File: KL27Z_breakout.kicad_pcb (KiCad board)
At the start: 2 copper layers, 12 x 55 mm, 15 parts, among them J1 USB_mini_micro_B, P1 CONN_01X08, P2 CONN_01X08, P3 CONN_01X08, P4 CONN_01X08, SW1 SW_PUSH, SW2 SW_PUSH, U1 MKL27Z256VFM4

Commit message: Save some works
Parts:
- P1, P2, P3, P4: footprint Pin_Headers:Pin_Header_Straight_1x08 -> keyboard_parts:Pin_Header_Straight_1x08
- moved C3 43.6 mm to (105.8, 138.5)
- moved C2 42.5 mm to (101.0, 129.5), turned to 90 degrees
- moved C4 41.8 mm to (101.0, 134.5), turned to 270 degrees
- moved SW1 39.7 mm to (106.0, 155.0), turned to 270 degrees
- moved SW2 35.6 mm to (106.0, 148.4), turned to 90 degrees
- moved C1 23.9 mm to (102.1, 106.0), turned to 0 degrees
- moved R1 16.3 mm to (105.0, 124.0)
- moved R2 16.3 mm to (107.0, 124.0)
- moved P2 12.2 mm to (102.2, 147.1)
- moved P1 9.19 mm to (102.2, 116.9)
- moved P4 8.81 mm to (109.8, 116.9)
- moved P3 6.06 mm to (109.8, 147.1)
- moved U1 2.42 mm to (106.0, 132.0)
- moved SJ1 0.16 mm to (104.0, 109.3)
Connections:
- P1 pad 8: PTE0 -> (no net)
- P2 pad 8: GND -> PTA18
- P3 pad 1: PTA18 -> PTA19
- P3 pad 2: PTA19 -> PTA20
- P3 pad 3: PTA20 -> PTB0
- P3 pad 4: PTB0 -> PTB1
- P3 pad 5: PTB1 -> PTC1
- P3 pad 6: PTC1 -> PTC2
- P3 pad 7: PTC2 -> PTC3
- P3 pad 8: PTC3 -> PTC4
- P4 pad 1: PTC4 -> PTC5
- P4 pad 2: PTC5 -> PTC6
- P4 pad 3: PTC6 -> PTC7
- P4 pad 4: PTC7 -> PTD4
- P4 pad 5: PTD4 -> PTD5
- P4 pad 6: PTD5 -> PTD6
- P4 pad 7: PTD6 -> PTD7
- P4 pad 8: PTD7 -> PTE0
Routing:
- net PTE0: track 4.33 -> 25.1 mm
- net Net-(J1-Pad2): track 0.00 -> 19.5 mm
- net Net-(J1-Pad3): track 0.00 -> 19.4 mm
- net +3V3: track 0.07 -> 16.4 mm, vias 0 -> 1
- net PTD4: track 0.00 -> 15.1 mm, vias 0 -> 1
- net Net-(R1-Pad1): track 20.0 -> 5.40 mm, vias 0 -> 2
- net PTC7: track 0.00 -> 13.3 mm, vias 0 -> 1
- net Net-(R2-Pad1): track 20.3 -> 7.76 mm
- net PTC6: track 0.00 -> 11.1 mm, vias 0 -> 1
- net PTC4: track 0.00 -> 7.92 mm
- net PTC5: track 0.00 -> 7.53 mm, vias 0 -> 1
- net VBUS: track 0.00 -> 6.96 mm
- net PTA19: track 20.9 -> 25.6 mm
- net VREGIN: track 21.2 -> 25.6 mm, vias 0 -> 1
- net PTC3: track 7.27 -> 11.5 mm, vias 0 -> 1
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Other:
- board size 12 x 55 mm -> 12 x 60 mm

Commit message: 400mil pcb
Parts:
- P1, P4: value CONN_01X08 -> CONN_01X06; footprint keyboard_parts:Pin_Header_Straight_1x08 -> keyboard_parts:Pin_Header_Straight_1x06
- moved C2 21.9 mm to (103.2, 107.7)
- moved R1 20.4 mm to (107.3, 103.7)
- moved R2 20.3 mm to (105.3, 103.7)
- moved SW2 19.5 mm to (105.1, 129.0)
- moved SW1 19.0 mm to (105.1, 136.1)
- moved P2 18.0 mm to (100.0, 129.2)
- moved C4 18.0 mm to (99.9, 116.5)
- moved P3 17.9 mm to (110.2, 129.2)
- moved U1 15.5 mm to (105.1, 116.5)
- moved C3 15.3 mm to (104.6, 123.2), turned to 270 degrees
- moved P1 10.8 mm to (100.0, 106.3)
- moved P4 10.5 mm to (110.2, 106.3)
- moved SJ1 8.40 mm to (101.5, 101.3)
- moved J1 6.63 mm to (105.1, 94.9)
- moved C1 2.52 mm to (103.2, 103.7), turned to 270 degrees
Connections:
- J1 pad 4: (no net) -> Net-(J1-Pad4)
- P1 pad 3: +3V3 -> PTD5
- P1 pad 4: PTA0 -> PTD6
- P1 pad 5: PTA3 -> PTD7
- P1 pad 6: PTA20 -> PTE0
- P3 pad 8: PTC4 -> GND
- P4 pad 1: PTC5 -> PTC4
- P4 pad 2: PTC6 -> PTC5
- P4 pad 3: PTC7 -> PTC6
- P4 pad 4: PTD4 -> PTC7
- P4 pad 5: PTD5 -> PTD4
- P4 pad 6: PTD6 -> GND
- U1 pad 33: (no net) -> GND
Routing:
- net GND: track 1.19 -> 80.7 mm, vias 1 -> 22
- net PTE0: track 25.1 -> 4.98 mm
- net Net-(J1-Pad3): track 19.4 -> 5.38 mm, vias 0 -> 2
- net PTD7: track 21.7 -> 8.04 mm
- net Net-(J1-Pad2): track 19.5 -> 7.25 mm
- net +3V3: track 16.4 -> 26.3 mm, vias 1 -> 3
- net PTD6: track 19.9 -> 11.7 mm
- net VREGIN: track 25.6 -> 18.9 mm, vias 1 -> 0
- net Net-(R1-Pad1): track 5.40 -> 11.9 mm, vias 2 -> 0
- net PTC3: track 11.5 -> 7.45 mm, vias 1 -> 0
- net PTC2: track 13.4 -> 9.71 mm, vias 1 -> 0
- net PTA0: track 13.4 -> 10.0 mm
- net Net-(R2-Pad1): track 7.76 -> 11.1 mm
- net PTA2: track 18.0 -> 14.7 mm
- net PTA3: track 20.3 -> 17.0 mm
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- added copper zone on B.Cu, net GND
- added copper zone on F.Cu, net GND
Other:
- board size 12 x 60 mm -> 13.7 x 46.4 mm

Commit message: Save 300mil work
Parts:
- moved C3 12.1 mm to (92.6, 121.1)
- moved C1 10.3 mm to (93.1, 105.6)
- moved C2 8.93 mm to (94.9, 110.9)
- moved C4 7.24 mm to (92.6, 116.5)
- moved P3 3.59 mm to (107.6, 131.8)
- moved SW2 3.54 mm to (103.8, 132.3)
- moved SW1 3.07 mm to (103.8, 138.9)
- moved P4 2.84 mm to (107.6, 107.6)
- moved U1 2.84 mm to (103.8, 119.0)
- moved R1 2.70 mm to (104.8, 104.8)
- moved R2 2.70 mm to (102.8, 104.8)
- moved P2 2.54 mm to (100.0, 131.8)
- moved P1 1.27 mm to (100.0, 107.6)
- moved J1 1.27 mm to (103.8, 94.9)
- moved SJ1 0.76 mm to (102.3, 101.3)
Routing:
- net (no net): track 0.00 -> 464.9 mm, vias 0 -> 31
- net GND: track 80.7 -> 0.00 mm, vias 22 -> 0
- net +3V3: track 26.3 -> 0.00 mm, vias 3 -> 0
- net PTA19: track 22.8 -> 0.00 mm
- net PTA18: track 22.6 -> 0.00 mm
- net PTA20: track 20.8 -> 0.00 mm
- net PTA4: track 19.7 -> 0.00 mm
- net VREGIN: track 18.9 -> 0.00 mm
- net PTB0: track 17.4 -> 0.00 mm
- net PTA3: track 17.0 -> 0.00 mm
- net PTD5: track 15.1 -> 0.00 mm, vias 1 -> 0
- net PTB1: track 15.0 -> 0.00 mm
- net PTA2: track 14.7 -> 0.00 mm
- net PTD4: track 14.2 -> 0.00 mm
- net PTA1: track 12.3 -> 0.00 mm
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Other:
- board size 13.7 x 46.4 mm -> 13.8 x 46.4 mm

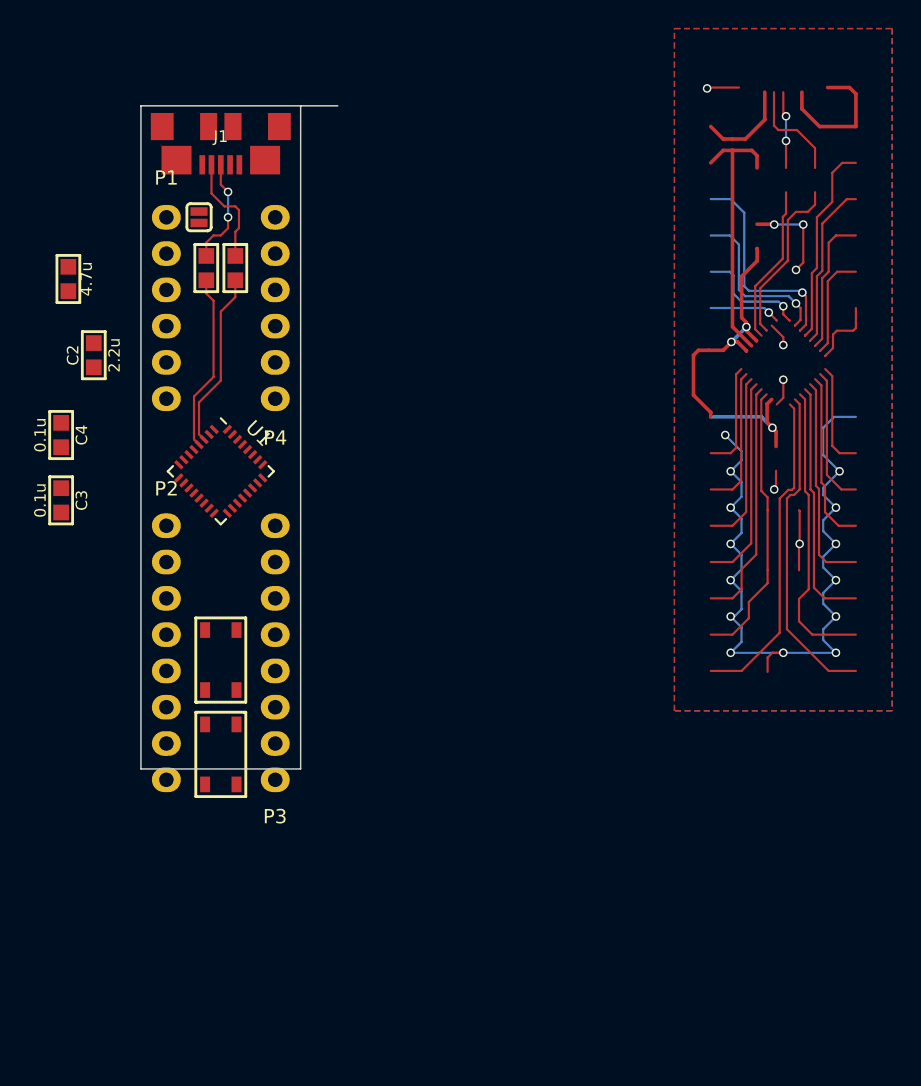
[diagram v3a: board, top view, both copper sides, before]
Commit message: Route traces for 300mil PCB
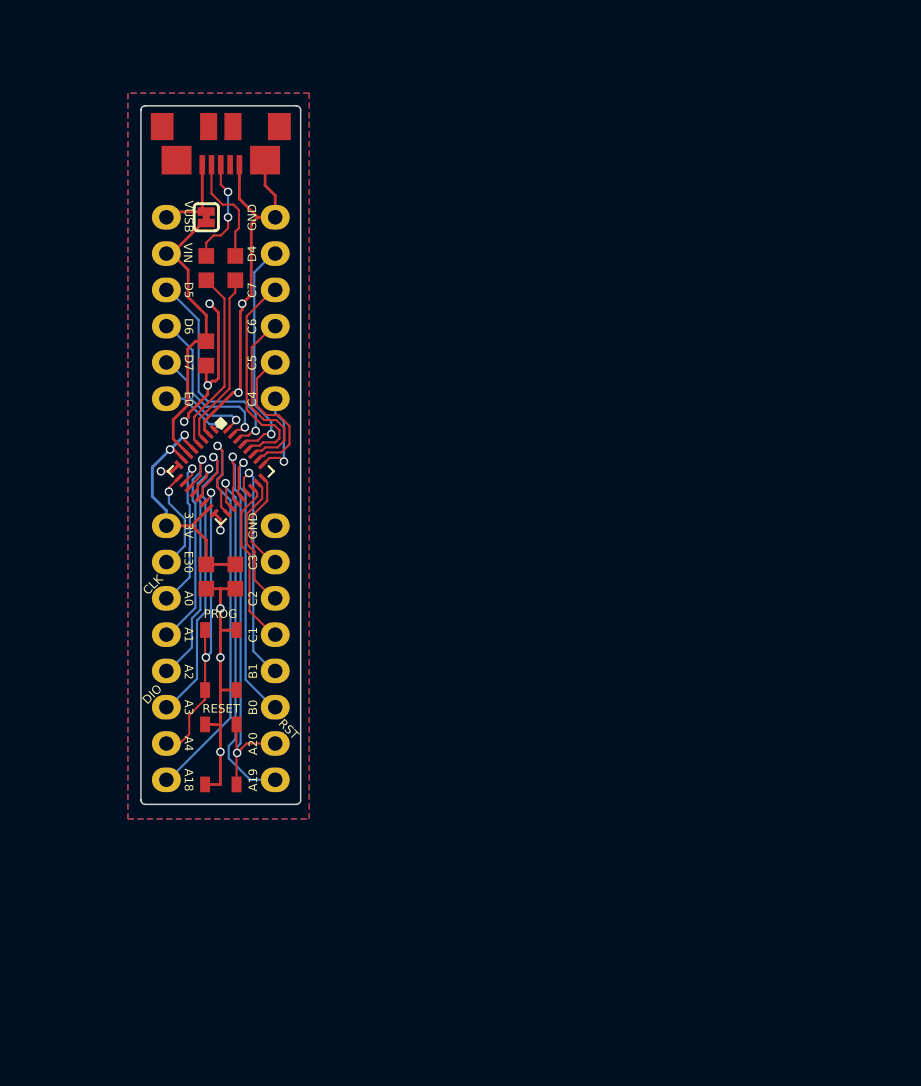
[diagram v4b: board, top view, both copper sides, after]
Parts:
- removed C3: 0.1u, keyboard_parts:C_1608
- SJ1: footprint keyboard_parts:SOLDER_JUMPER_2 -> keyboard_parts:SOLDER_JUMPER_2_WIRED
- moved C2 17.4 mm to (102.8, 126.4), turned to 270 degrees
- moved C4 15.7 mm to (104.8, 126.4)
- moved C1 11.0 mm to (102.8, 110.8)
- moved SJ1 0.51 mm to (102.8, 101.3)
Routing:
- net (no net): track 464.9 -> 0.00 mm, vias 31 -> 0
- net GND: track 0.00 -> 62.1 mm, vias 0 -> 10
- net PTA20: track 0.00 -> 31.7 mm, vias 0 -> 2
- net PTA18: track 0.00 -> 31.3 mm, vias 0 -> 1
- net PTA19: track 0.00 -> 25.6 mm, vias 0 -> 1
- net PTA3: track 0.00 -> 22.9 mm, vias 0 -> 1
- net PTA4: track 0.00 -> 22.3 mm, vias 0 -> 2
- net PTB0: track 0.00 -> 21.1 mm, vias 0 -> 1
- net VREGIN: track 0.00 -> 20.6 mm
- net +3V3: track 0.00 -> 19.0 mm, vias 0 -> 2
- net PTA2: track 0.00 -> 17.8 mm, vias 0 -> 1
- net PTB1: track 0.00 -> 16.4 mm, vias 0 -> 1
- net PTD4: track 0.00 -> 16.1 mm, vias 0 -> 1
- net PTA1: track 0.00 -> 15.9 mm, vias 0 -> 1
- net PTD5: track 0.00 -> 15.6 mm, vias 0 -> 1
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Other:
- board size 13.8 x 46.4 mm -> 11.2 x 48.9 mm
- rule pad_to_mask_clearance: 0.2 -> 0.05
- board text added: "3.3V"
- board text added: "A0"
- board text added: "A1"
- board text added: "A18"
- board text added: "A19"
- board text added: "A2"
- board text added: "A20"
- board text added: "A3"
- board text added: "A4"
- board text added: "B0"
- board text added: "B1"
- board text added: "C1"
- board text added: "C2"
- board text added: "C3"
- board text added: "C4"
- board text added: "C5"
- board text added: "C6"
- board text added: "C7"
- board text added: "CLK"
- board text added: "D4"
- board text added: "D5"
- board text added: "D6"
- board text added: "D7"
- board text added: "DIO"
- board text added: "E0"
- board text added: "E30"
- board text added: "GND"
- board text added: "KL27Z breakout TMK 2016/07"
- board text added: "PROG"
- board text added: "RESET"
- board text added: "RST"
- board text added: "VIN"
- board text added: "VUSB"

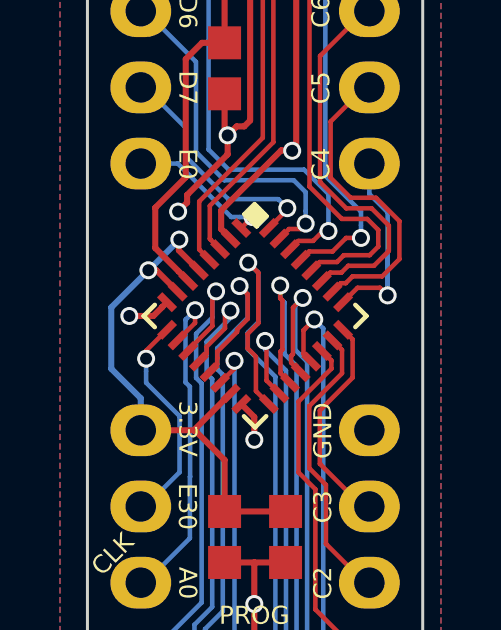
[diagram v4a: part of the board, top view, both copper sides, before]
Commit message: Add silk screen fill under thermal pad
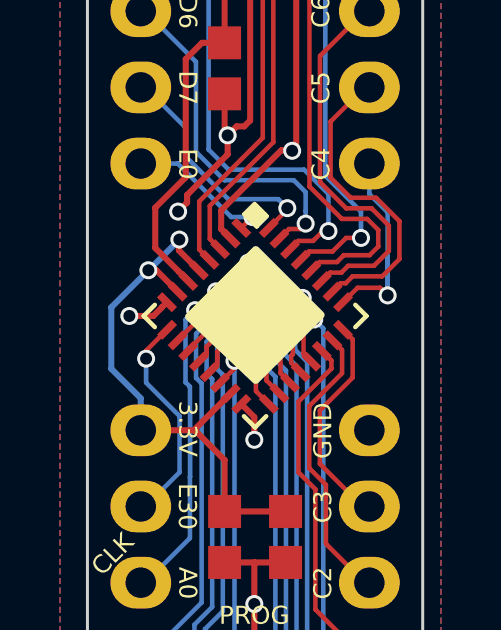
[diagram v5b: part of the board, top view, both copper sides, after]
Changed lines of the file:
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@@
   (general
     (links 57)
-    (no_connects 1)
-    (area 94.881667 86.8546 120.440115 145.865)
+    (no_connects 0)
+    (area 98.171999 93.419999 109.448001 142.410001)
     (thickness 1.6)
     (drawings 72)
@@
     (34 B.Paste user)
     (35 F.Paste user)
-    (36 B.SilkS user hide)
+    (36 B.SilkS user)
     (37 F.SilkS user)
     (38 B.Mask user)
@@
     (visible_elements FFFFEF7F)
     (pcbplotparams
-      (layerselection 0x010f8_80000001)
+      (layerselection 0x010f0_80000001)
       (usegerberextensions true)
       (excludeedgelayer true)
@@
     (add_net VBUS)
     (add_net VREGIN)
-  )
-  (module keyboard_parts:USB_microB (layer F.Cu)
-    (at 103.81 94.92 180)
-    (descr "USB microB hirose ZX62R-B-5P")
-    (tags "USB micorB hirose")
-    (fp_text reference J1 (at 0 -0.6985 180) (layer F.SilkS) hide
-      (effects (font (size 0.8128 0.8128) (thickness 0.2032)))
-    )
-    (fp_text value USB_mini_micro_B (at 0 0.22606 180) (layer F.SilkS) hide
-      (effects (font (size 0.6 0.6) (thickness 0.15)))
-    )
-    (fp_text user "PCB edge" (at -0.05 1.45 180) (layer Dwgs.User) hide
-      (effects (font (size 0.5 0.5) (thickness 0.125)))
-    )
-    (fp_line (start 3.75 2.15) (end 4.25 2.75) (layer Dwgs.User) (width 0.2))
-    (fp_line (start -3.75 2.15) (end -4.25 2.675) (layer Dwgs.User) (width 0.2))
-    (fp_line (start -3 1.45) (end 3 1.45) (layer Dwgs.User) (width 0.2))
-    (fp_line (start -3.75 2.15) (end -3.75 1.35) (layer Dwgs.User) (width 0.2))
-    (fp_line (start -3.75 2.15) (end 3.75 2.15) (layer Dwgs.User) (width 0.2))
-    (fp_line (start 3.75 2.15) (end 3.75 1.35) (layer Dwgs.User) (width 0.2))
-    (pad 6 smd rect (at 0.85 0 180) (size 1.2 1.9) (layers F.Cu F.Paste F.Mask))
-    (pad 1 smd rect (at 1.29794 -2.67462) (size 0.4 1.35) (layers F.Cu F.Paste F.Mask)
-      (net 4 VBUS) (clearance 0.1))
-    (pad 6 smd rect (at -3.0988 -2.3495 180) (size 2.1 2) (layers F.Cu F.Paste F.Mask)
-      (net 1 GND))
-    (pad 6 smd rect (at 3.0988 -2.3495 180) (size 2.1 2) (layers F.Cu F.Paste F.Mask)
-      (net 1 GND))
-    (pad 6 smd rect (at -4.09956 0 180) (size 1.6 1.9) (layers F.Cu F.Paste F.Mask)
-      (net 1 GND))
-    (pad 6 smd rect (at 4.09956 0 180) (size 1.6 1.9) (layers F.Cu F.Paste F.Mask)
-      (net 1 GND))
-    (pad 2 smd rect (at 0.65024 -2.67462) (size 0.4 1.35) (layers F.Cu F.Paste F.Mask)
-      (net 5 "Net-(J1-Pad2)") (clearance 0.1))
-    (pad 3 smd rect (at 0 -2.67462) (size 0.4 1.35) (layers F.Cu F.Paste F.Mask)
-      (net 6 "Net-(J1-Pad3)") (clearance 0.1))
-    (pad 4 smd rect (at -0.65024 -2.67462) (size 0.4 1.35) (layers F.Cu F.Paste F.Mask)
-      (net 32 "Net-(J1-Pad4)") (clearance 0.1))
-    (pad 5 smd rect (at -1.30048 -2.67462) (size 0.4 1.35) (layers F.Cu F.Paste F.Mask)
-      (net 1 GND) (clearance 0.1))
-    (pad 6 smd rect (at -0.85 0 180) (size 1.2 1.9) (layers F.Cu F.Paste F.Mask))
   )
   (module Housings_DFN_QFN:QFN-32-1EP_5x5mm_Pitch0.5mm locked (layer F.Cu)
@@
     (pad 32 smd rect (at -1.75 -2.4 45) (size 0.7 0.25) (layers F.Cu F.Paste F.Mask)
       (net 29 PTD7))
-    (pad "" smd rect (at 0 0 315) (size 3.5 3.5) (layers F.SilkS))
     (model Housings_DFN_QFN.3dshapes/QFN-32-1EP_5x5mm_Pitch0.5mm.wrl
       (at (xyz 0 0 0))
@@
       (rotate (xyz 0 0 0))
     )
+  )
+  (module keyboard_parts:USB_microB (layer F.Cu)
+    (at 103.81 94.92 180)
+    (descr "USB microB hirose ZX62R-B-5P")
+    (tags "USB micorB hirose")
+    (fp_text reference J1 (at 0 -0.6985 180) (layer F.SilkS) hide
+      (effects (font (size 0.8128 0.8128) (thickness 0.2032)))
+    )
+    (fp_text value USB_mini_micro_B (at 0 0.22606 180) (layer F.SilkS) hide
+      (effects (font (size 0.6 0.6) (thickness 0.15)))
+    )
+    (fp_text user "PCB edge" (at -0.05 1.45 180) (layer Dwgs.User) hide
+      (effects (font (size 0.5 0.5) (thickness 0.125)))
+    )
+    (fp_line (start 3.75 2.15) (end 4.25 2.75) (layer Dwgs.User) (width 0.2))
+    (fp_line (start -3.75 2.15) (end -4.25 2.675) (layer Dwgs.User) (width 0.2))
+    (fp_line (start -3 1.45) (end 3 1.45) (layer Dwgs.User) (width 0.2))
+    (fp_line (start -3.75 2.15) (end -3.75 1.35) (layer Dwgs.User) (width 0.2))
+    (fp_line (start -3.75 2.15) (end 3.75 2.15) (layer Dwgs.User) (width 0.2))
+    (fp_line (start 3.75 2.15) (end 3.75 1.35) (layer Dwgs.User) (width 0.2))
+    (pad 6 smd rect (at 0.85 0 180) (size 1.2 1.9) (layers F.Cu F.Paste F.Mask))
+    (pad 1 smd rect (at 1.29794 -2.67462) (size 0.4 1.35) (layers F.Cu F.Paste F.Mask)
+      (net 4 VBUS) (clearance 0.1))
+    (pad 6 smd rect (at -3.0988 -2.3495 180) (size 2.1 2) (layers F.Cu F.Paste F.Mask)
+      (net 1 GND))
+    (pad 6 smd rect (at 3.0988 -2.3495 180) (size 2.1 2) (layers F.Cu F.Paste F.Mask)
+      (net 1 GND))
+    (pad 6 smd rect (at -4.09956 0 180) (size 1.6 1.9) (layers F.Cu F.Paste F.Mask)
+      (net 1 GND))
+    (pad 6 smd rect (at 4.09956 0 180) (size 1.6 1.9) (layers F.Cu F.Paste F.Mask)
+      (net 1 GND))
+    (pad 2 smd rect (at 0.65024 -2.67462) (size 0.4 1.35) (layers F.Cu F.Paste F.Mask)
+      (net 5 "Net-(J1-Pad2)") (clearance 0.1))
+    (pad 3 smd rect (at 0 -2.67462) (size 0.4 1.35) (layers F.Cu F.Paste F.Mask)
+      (net 6 "Net-(J1-Pad3)") (clearance 0.1))
+    (pad 4 smd rect (at -0.65024 -2.67462) (size 0.4 1.35) (layers F.Cu F.Paste F.Mask)
+      (net 32 "Net-(J1-Pad4)") (clearance 0.1))
+    (pad 5 smd rect (at -1.30048 -2.67462) (size 0.4 1.35) (layers F.Cu F.Paste F.Mask)
+      (net 1 GND) (clearance 0.1))
+    (pad 6 smd rect (at -0.85 0 180) (size 1.2 1.9) (layers F.Cu F.Paste F.Mask))
   )
   (module keyboard_parts:C_1608 placed (layer F.Cu)
@@
       )
     )
+  )
+  (zone (net 0) (net_name "") (layer F.SilkS) (hatch edge 0.508)
+    (connect_pads (clearance 0.2))
+    (min_thickness 0.254)
+    (fill yes (arc_segments 16) (thermal_gap 0.508) (thermal_bridge_width 0.508))
+    (polygon
+      (pts
+        (xy 103.8326 116.6667) (xy 106.1821 119.0162) (xy 103.8326 121.3657) (xy 101.4196 119.0797)
+      )
+    )

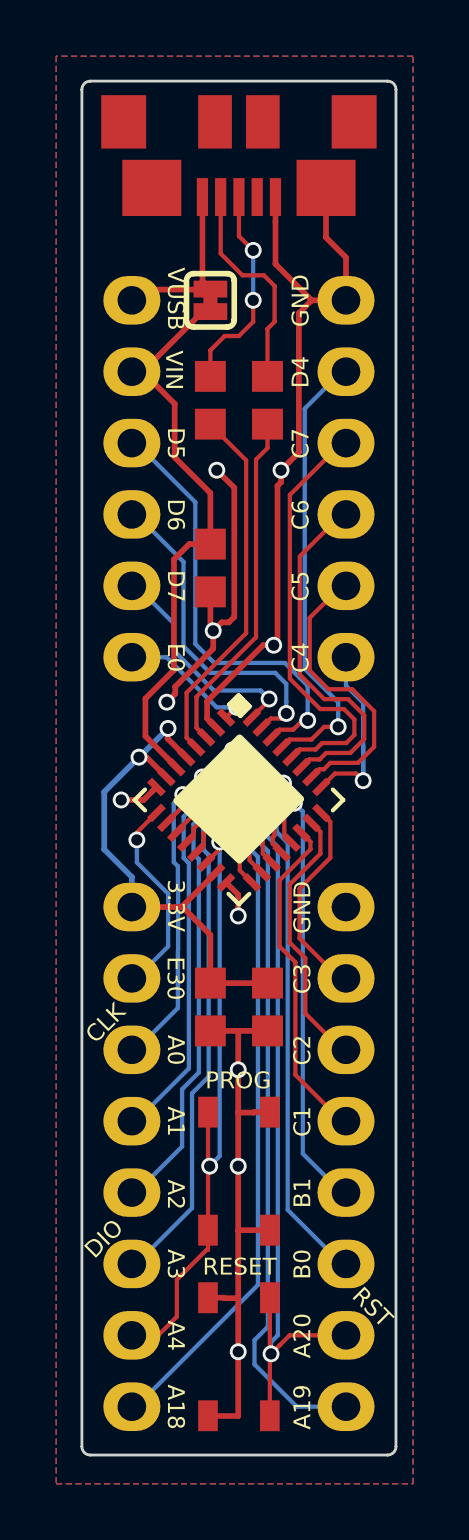
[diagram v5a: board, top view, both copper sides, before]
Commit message: Fix D- and D+ lines and pin header position
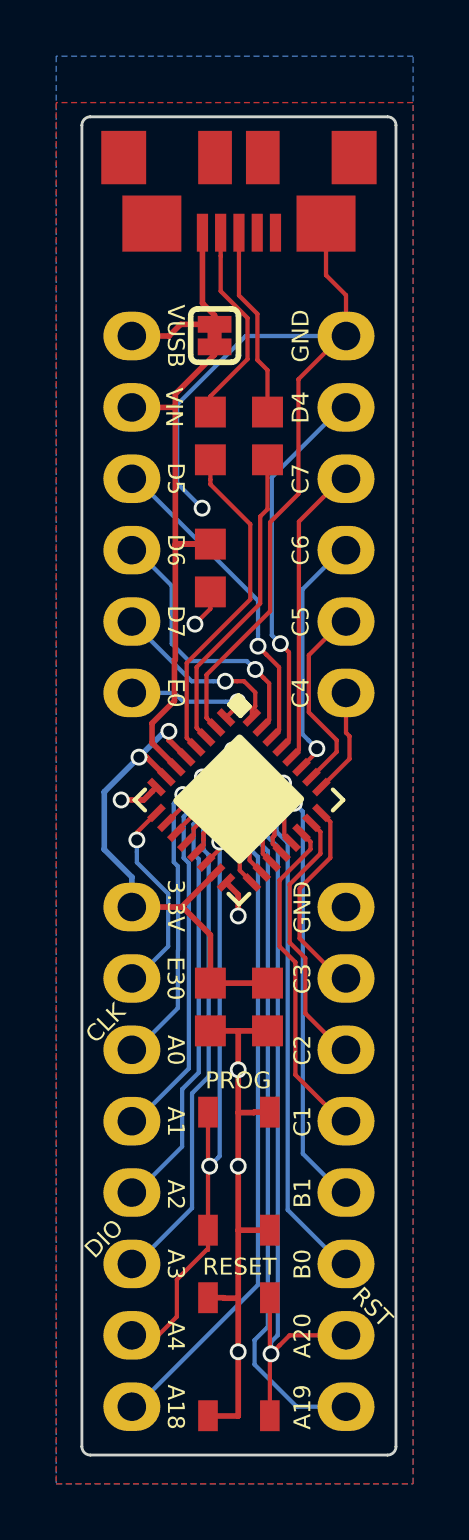
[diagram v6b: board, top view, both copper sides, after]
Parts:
- moved R1 1.27 mm to (104.8, 106.1)
- moved R2 1.27 mm to (102.8, 106.1)
- moved J1 1.27 mm to (103.8, 96.2)
- moved P1 1.27 mm to (100.0, 108.9)
- moved P4 1.27 mm to (107.6, 108.9)
- moved SJ1 1.26 mm to (102.9, 102.5)
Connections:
- R1 pad 2: Net-(J1-Pad2) -> Net-(J1-Pad3)
- R2 pad 2: Net-(J1-Pad3) -> Net-(J1-Pad2)
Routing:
- net GND: track 62.1 -> 55.9 mm, vias 10 -> 7
- net PTC7: track 15.3 -> 10.8 mm
- net PTD5: track 15.6 -> 11.6 mm
- net PTC6: track 12.9 -> 8.90 mm, vias 0 -> 1
- net PTC4: track 7.71 -> 3.82 mm, vias 1 -> 0
- net PTC5: track 10.5 -> 6.94 mm
- net PTD4: track 16.1 -> 13.6 mm
- net PTD6: track 11.9 -> 9.74 mm
- net PTD7: track 8.03 -> 6.38 mm
- net Net-(R1-Pad1): track 12.3 -> 11.1 mm
- net Net-(R2-Pad1): track 13.0 -> 11.9 mm
- net Net-(J1-Pad3): track 7.52 -> 6.80 mm, vias 2 -> 0
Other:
- board size 11.2 x 48.9 mm -> 11.2 x 47.6 mm
